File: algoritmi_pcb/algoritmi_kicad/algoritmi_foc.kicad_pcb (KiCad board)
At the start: 2 copper layers, 45.2 x 29.2 mm, 23 parts, among them J1 SSM-107-L-DV-P-TR, J2 53261-0371, J3 SSM-105-L-SH, U1 TMC6300-LA-T

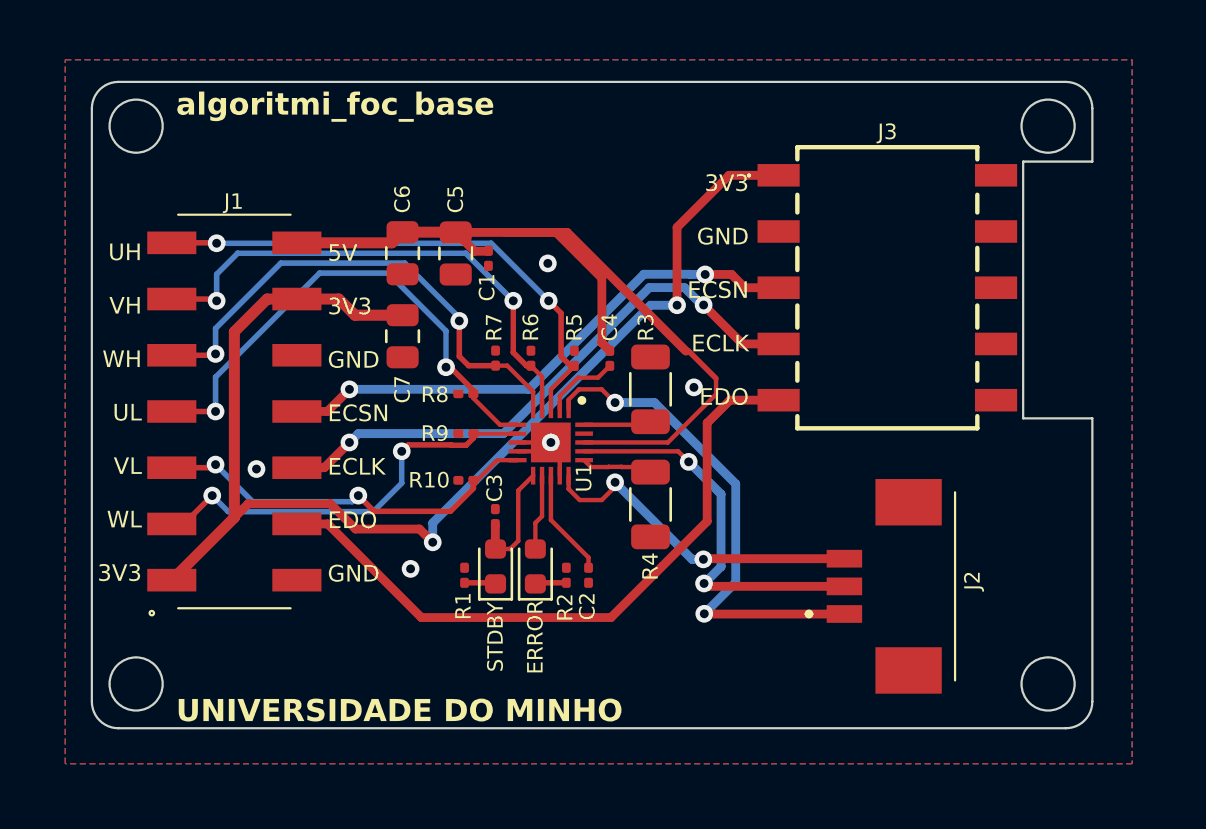
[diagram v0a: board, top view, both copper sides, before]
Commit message: generated BOMs and Gerbers
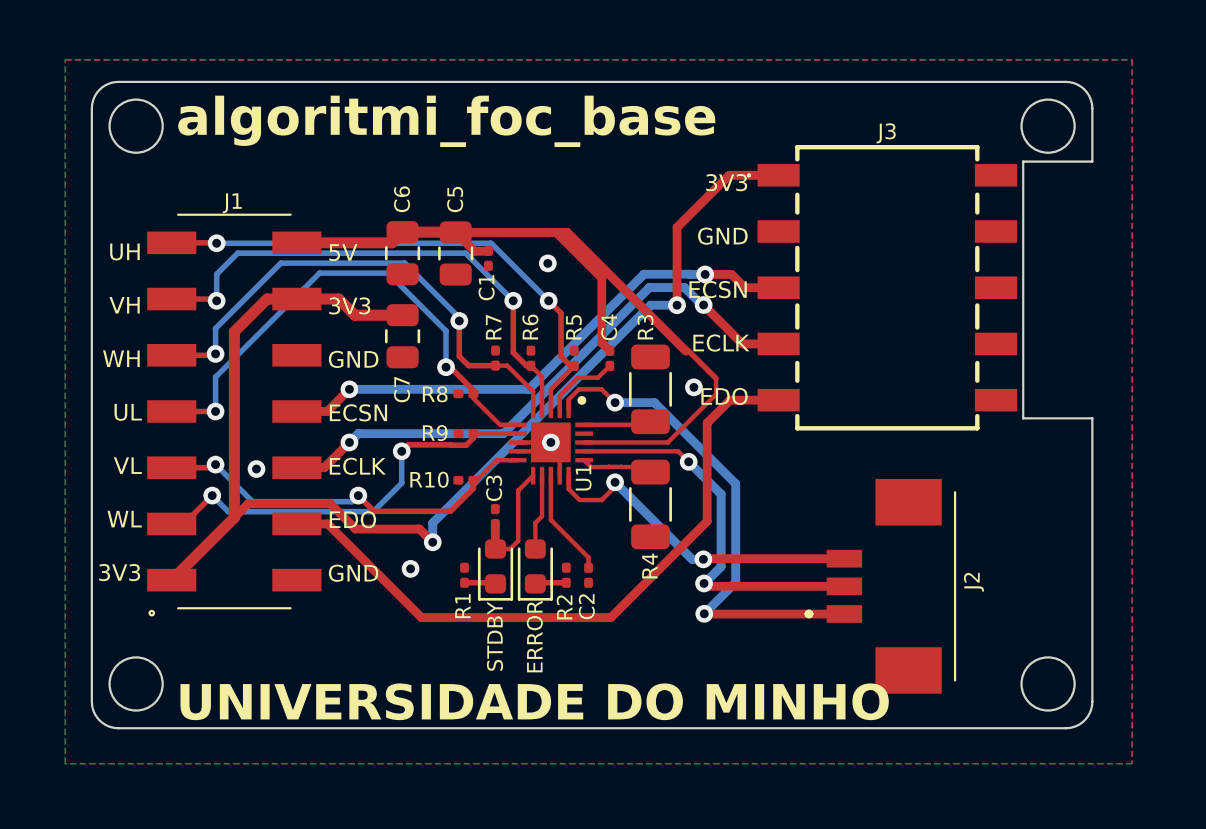
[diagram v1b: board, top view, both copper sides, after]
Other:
- board text added: "M2"
- board text removed: "SMARTKNOB"

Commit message: Updated Gerbers Base PCB
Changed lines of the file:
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@@
 			(drillshape 0)
 			(scaleselection 1)
-			(outputdirectory "algoritmi_foc_gerber/algoritmi_foc_map/")
+			(outputdirectory "algoritmi_foc_gerber/")
 		)
 	)
@@
 	)
 	(zone
-		(net 0)
-		(net_name "")
+		(net 1)
+		(net_name "GND")
 		(layer "F.Cu")
-		(name "a")
 		(hatch edge 0.5)
 		(connect_pads
@@
 		(min_thickness 0.25)
 		(filled_areas_thickness no)
-		(keepout
-			(tracks allowed)
-			(vias allowed)
-			(pads allowed)
-			(copperpour not_allowed)
-			(footprints allowed)
-		)
-		(fill
+		(fill yes
 			(thermal_gap 0.5)
 			(thermal_bridge_width 0.5)
@@
 		(polygon
 			(pts
-				(xy 84.4 85) (xy 84.4 86.4) (xy 84.6 86.4) (xy 85.2 85.8) (xy 85.2 85.4) (xy 85.4 85.2) (xy 85.8 85.2)
-				(xy 85.8 84.8) (xy 85.6 84.6) (xy 85 84.6) (xy 85 85)
+				(xy 79 66) (xy 127.2 66) (xy 127.2 97.8) (xy 79 97.8)
 			)
 		)
 	)
 	(zone
-		(net 1)
-		(net_name "GND")
-		(layers "F&B.Cu")
+		(net 0)
+		(net_name "")
+		(layer "F.Cu")
+		(name "a")
 		(hatch edge 0.5)
 		(connect_pads
@@
 		(min_thickness 0.25)
 		(filled_areas_thickness no)
-		(fill yes
+		(keepout
+			(tracks allowed)
+			(vias allowed)
+			(pads allowed)
+			(copperpour not_allowed)
+			(footprints allowed)
+		)
+		(fill
 			(thermal_gap 0.5)
 			(thermal_bridge_width 0.5)
@@
 		(polygon
 			(pts
-				(xy 79 66) (xy 127.2 66) (xy 127.2 97.8) (xy 79 97.8)
+				(xy 84.4 85) (xy 84.4 86.4) (xy 84.6 86.4) (xy 85.2 85.8) (xy 85.2 85.4) (xy 85.4 85.2) (xy 85.8 85.2)
+				(xy 85.8 84.8) (xy 85.6 84.6) (xy 85 84.6) (xy 85 85)
 			)
 		)
@@
 			)
 		)
+	)
+	(zone
+		(net 1)
+		(net_name "GND")
+		(layer "B.Cu")
+		(hatch edge 0.5)
+		(priority 1)
+		(connect_pads
+			(clearance 0)
+		)
+		(min_thickness 0.25)
+		(filled_areas_thickness no)
+		(fill yes
+			(thermal_gap 0.5)
+			(thermal_bridge_width 0.5)
+		)
+		(polygon
+			(pts
+				(xy 78.7 65.4) (xy 128.55 65.3) (xy 128.45 98.6) (xy 78.05 98.75)
+			)
+		)
